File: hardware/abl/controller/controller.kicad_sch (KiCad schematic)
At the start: 39 parts, among them IC1 TCA6408ARSVR, IC2 TCA6408ARSVR, IC3 VEML6040A3OG, IC4 TXB0104RUT, J1 SFW20S-2STE1LF, J2 Conn_02x05_Odd_Even, J3 Conn_02x05_Odd_Even, J4 PRT-14417, J5 Conn_02x05_Odd_Even, J6 Conn_01x10_Pin, J7 Conn_01x10_Pin, Q2 AO3401A, Q4 AO3401A, U1 INA219AxD

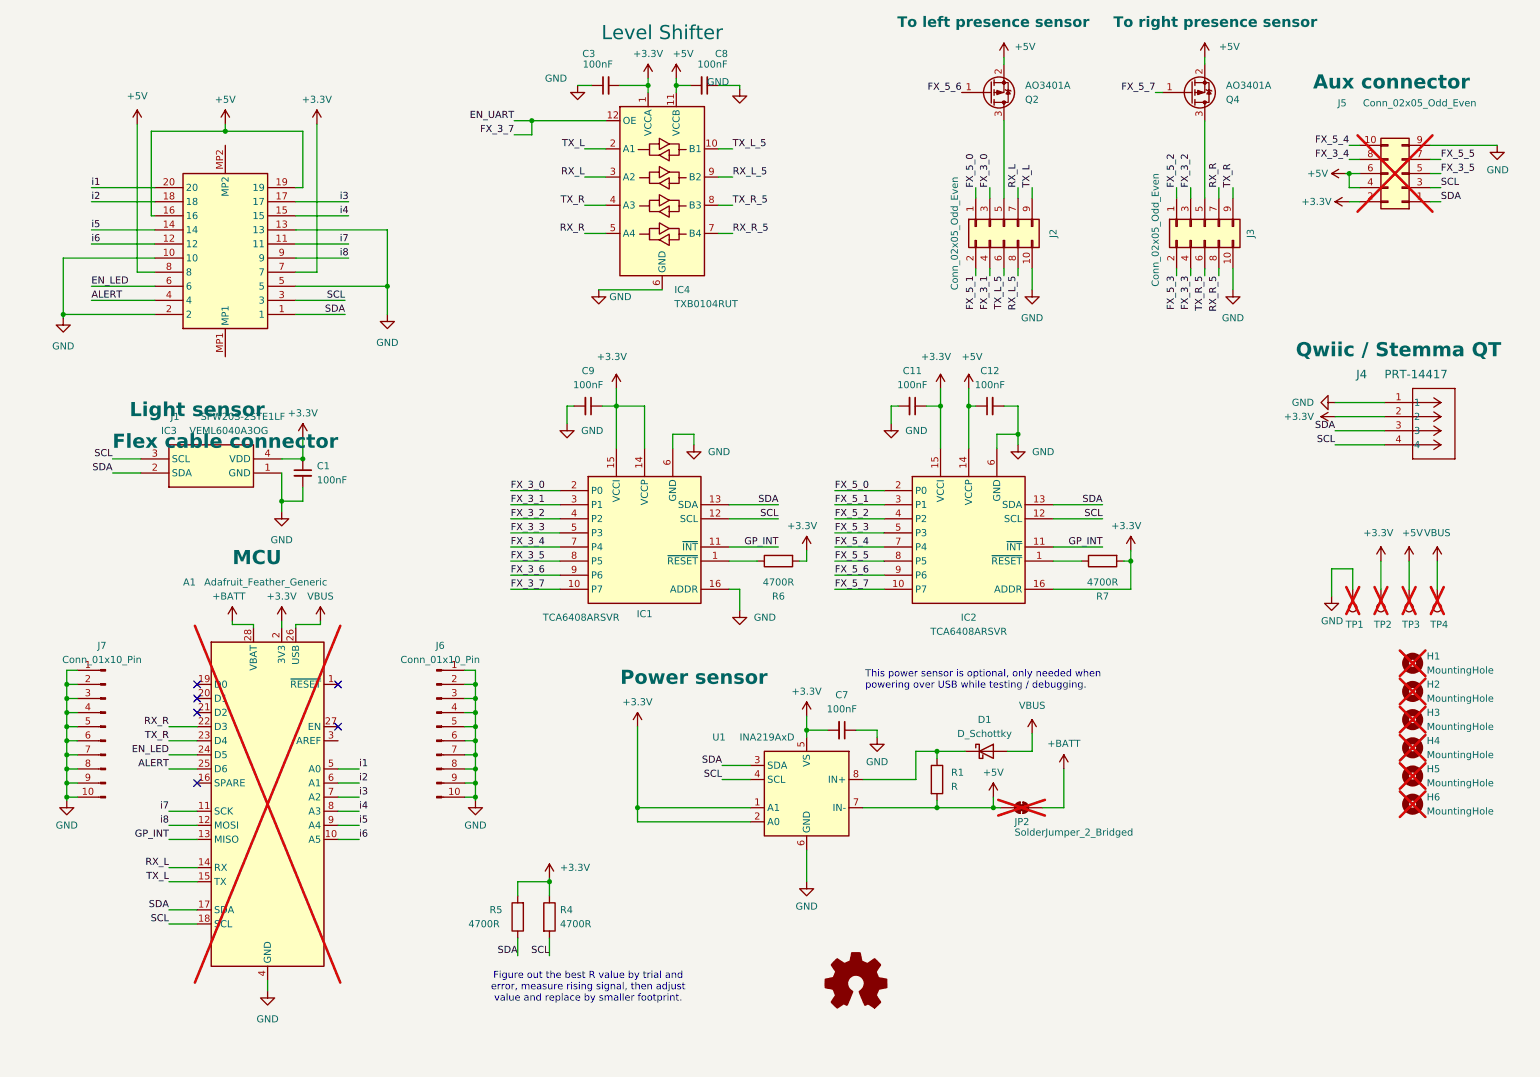
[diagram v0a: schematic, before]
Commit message: Relayout controller module for final pruction run.
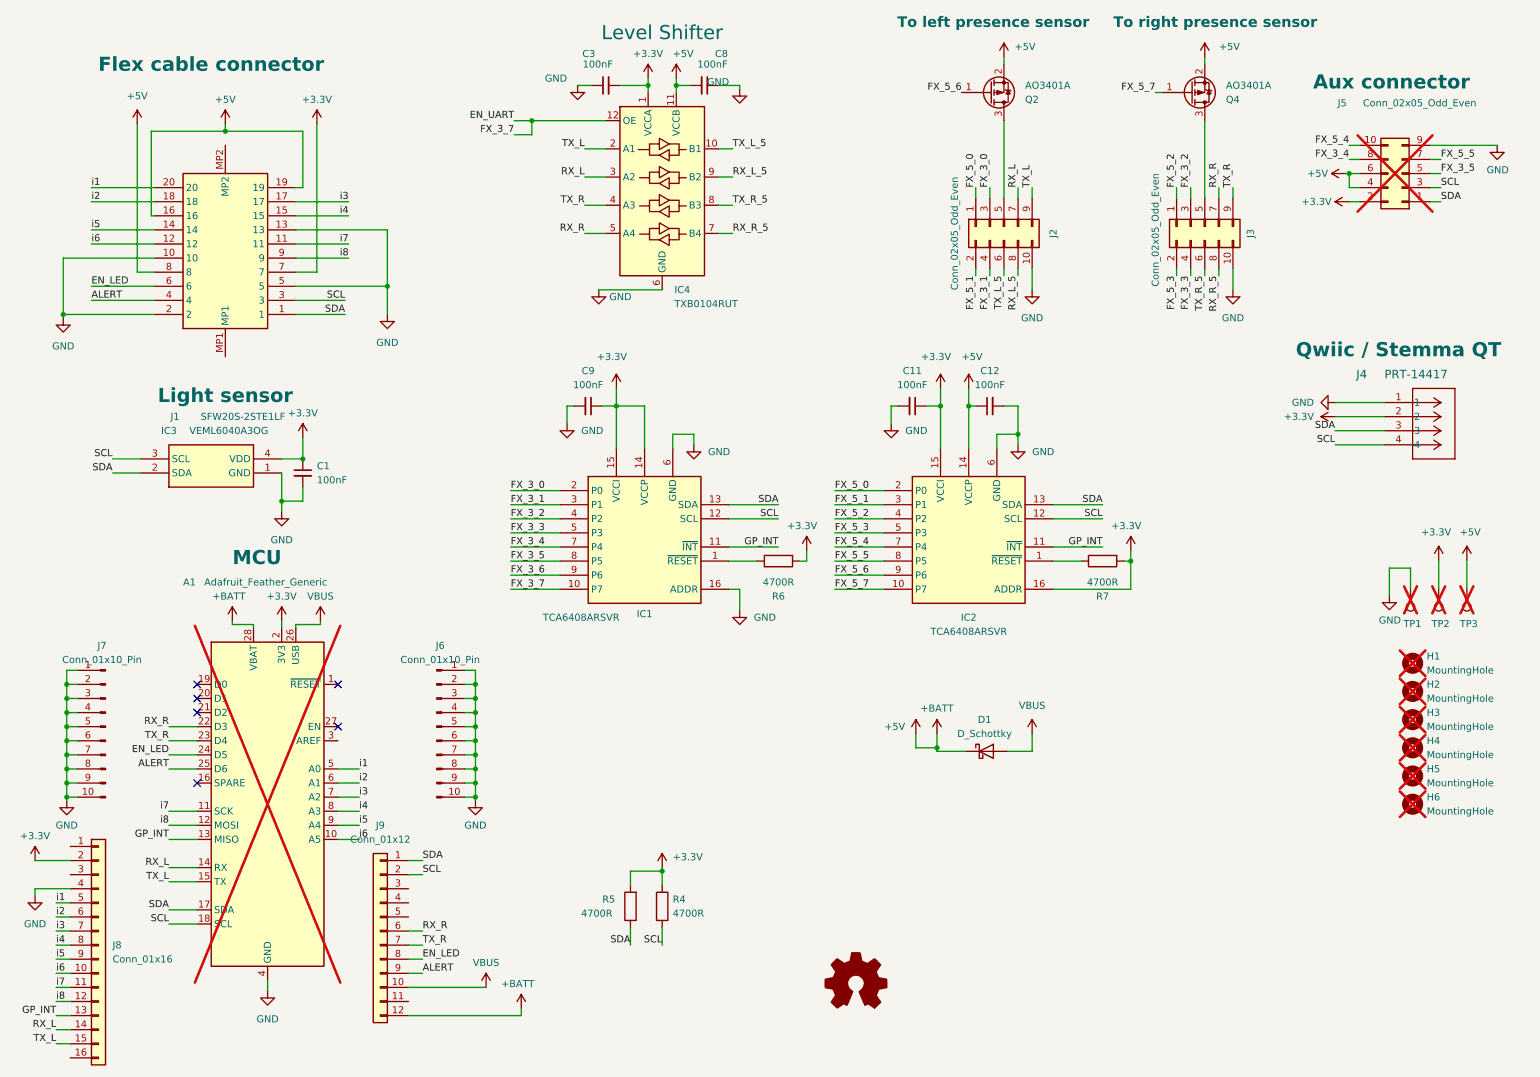
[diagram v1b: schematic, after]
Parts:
- removed C7: 100nF, Capacitor_SMD:C_0402_1005Metric, symbol Device:C_Small
- removed JP2: SolderJumper_2_Bridged, Jumper:SolderJumper-2_P1.3mm_Bridged2Bar_RoundedPad1.0x1.5mm, symbol Jumper:SolderJumper_2_Bridged
- removed R1: R, Resistor_SMD:R_2512_6332Metric, symbol Device:R
- removed TP4: TestPoint, TestPoint:TestPoint_THTPad_D1.5mm_Drill0.7mm, symbol Connector:TestPoint
- removed U1: INA219AxD, Package_SO:SOIC-8_3.9x4.9mm_P1.27mm, symbol Sensor_Energy:INA219AxD
- added J8: Conn_01x16, Connector_PinHeader_2.54mm:PinHeader_1x16_P2.54mm_Vertical, symbol Connector_Generic:Conn_01x16
- added J9: Conn_01x12, Connector_PinHeader_2.54mm:PinHeader_1x12_P2.54mm_Vertical, symbol Connector_Generic:Conn_01x12
- IC1, IC2: LCSC Part # (none) -> C2649390
- J2, J3: LCSC Part # (none) -> C29286622
- J6, J7: LCSC Part # (none) -> C42385486
- R4, R5: footprint Resistor_SMD:R_0805_2012Metric_Pad1.20x1.40mm_HandSolder -> Resistor_SMD:R_0402_1005Metric
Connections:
- net +BATT is gone; now on net +5V: A1.28 (VBAT)
- net +3.3V: now also J8.2 (Pin_2)
- net +5V: now also D1.1 (K), J9.12 (Pin_12)
- net ALERT: now also J9.9 (Pin_9)
- net EN_LED: now also J9.8 (Pin_8)
- net GND: now also J8.4 (Pin_4)
- net GP_INT: now also J8.13 (Pin_13)
- net RX_L: now also J8.14 (Pin_14)
- net RX_R: now also J9.6 (Pin_6)
- net SCL: now also J9.2 (Pin_2)
- net SDA: now also J9.1 (Pin_1)
- net TX_L: now also J8.15 (Pin_15)
- net TX_R: now also J9.7 (Pin_7)
- net VBUS: now also J9.10 (Pin_10)
- net i1: now also J8.5 (Pin_5)
- net i2: now also J8.6 (Pin_6)
- net i3: now also J8.7 (Pin_7)
- net i4: now also J8.8 (Pin_8)
- net i5: now also J8.9 (Pin_9)
- net i6: now also J8.10 (Pin_10)
- net i7: now also J8.11 (Pin_11)
- net i8: now also J8.12 (Pin_12)
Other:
- note removed: "Figure out the best R value by trial and error, measure rising signal, then adjust value and replace by smaller footprint."
- moved on the sheet: R4, R5, TP1, TP2, TP3

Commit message: Even more small adjustments before ordering v1.2 of controller module.
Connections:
- net +5V is gone; now on net +3.3V: A1.28 (VBAT), C12.1, C8.2, D1.1 (K), IC2.14 (VCCP), IC4.11 (VCCB), J1.16, J1.19, J1.8, J5.4 (Pin_4), J5.6 (Pin_6), J9.12 (Pin_12), Q2.2 (S), Q4.2 (S), TP3.1
- net GP_INT is gone; now on net GND: A1.13 (MISO), IC1.11 (~{INT}), IC2.11 (~{INT}), J8.13 (Pin_13)
- net RX_L is gone; now on net GND: A1.14 (RX), IC4.3 (A2), J2.7 (Pin_7), J8.14 (Pin_14)
- net SCL is gone; now on net GND: A1.18 (SCL), IC1.12 (SCL), IC2.12 (SCL), IC3.3 (SCL), J1.3, J4.4, J5.3 (Pin_3), J9.2 (Pin_2), R4.2
- net SDA is gone; now on net GND: A1.17 (SDA), IC1.13 (SDA), IC2.13 (SDA), IC3.2 (SDA), J1.1, J4.3, J5.1 (Pin_1), J9.1 (Pin_1), R5.1
- net TX_L is gone; now on net GND: A1.15 (TX), IC4.2 (A1), J2.9 (Pin_9), J8.15 (Pin_15)
- net TX_R is gone; now on net +3.3V: A1.23 (D4), IC4.4 (A3), J3.9 (Pin_9), J9.7 (Pin_7)
- net VBUS is gone; now on net +3.3V: A1.26 (USB), D1.2 (A), J9.10 (Pin_10)
- net i7 is gone; now on net GND: A1.11 (SCK), J1.11, J8.11 (Pin_11)
- net i8 is gone; now on net GND: A1.12 (MOSI), J1.9, J8.12 (Pin_12)
- net +3.3V: now also A1.3 (AREF)
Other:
- moved on the sheet: A1
